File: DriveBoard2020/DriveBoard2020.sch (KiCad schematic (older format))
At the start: 3 parts

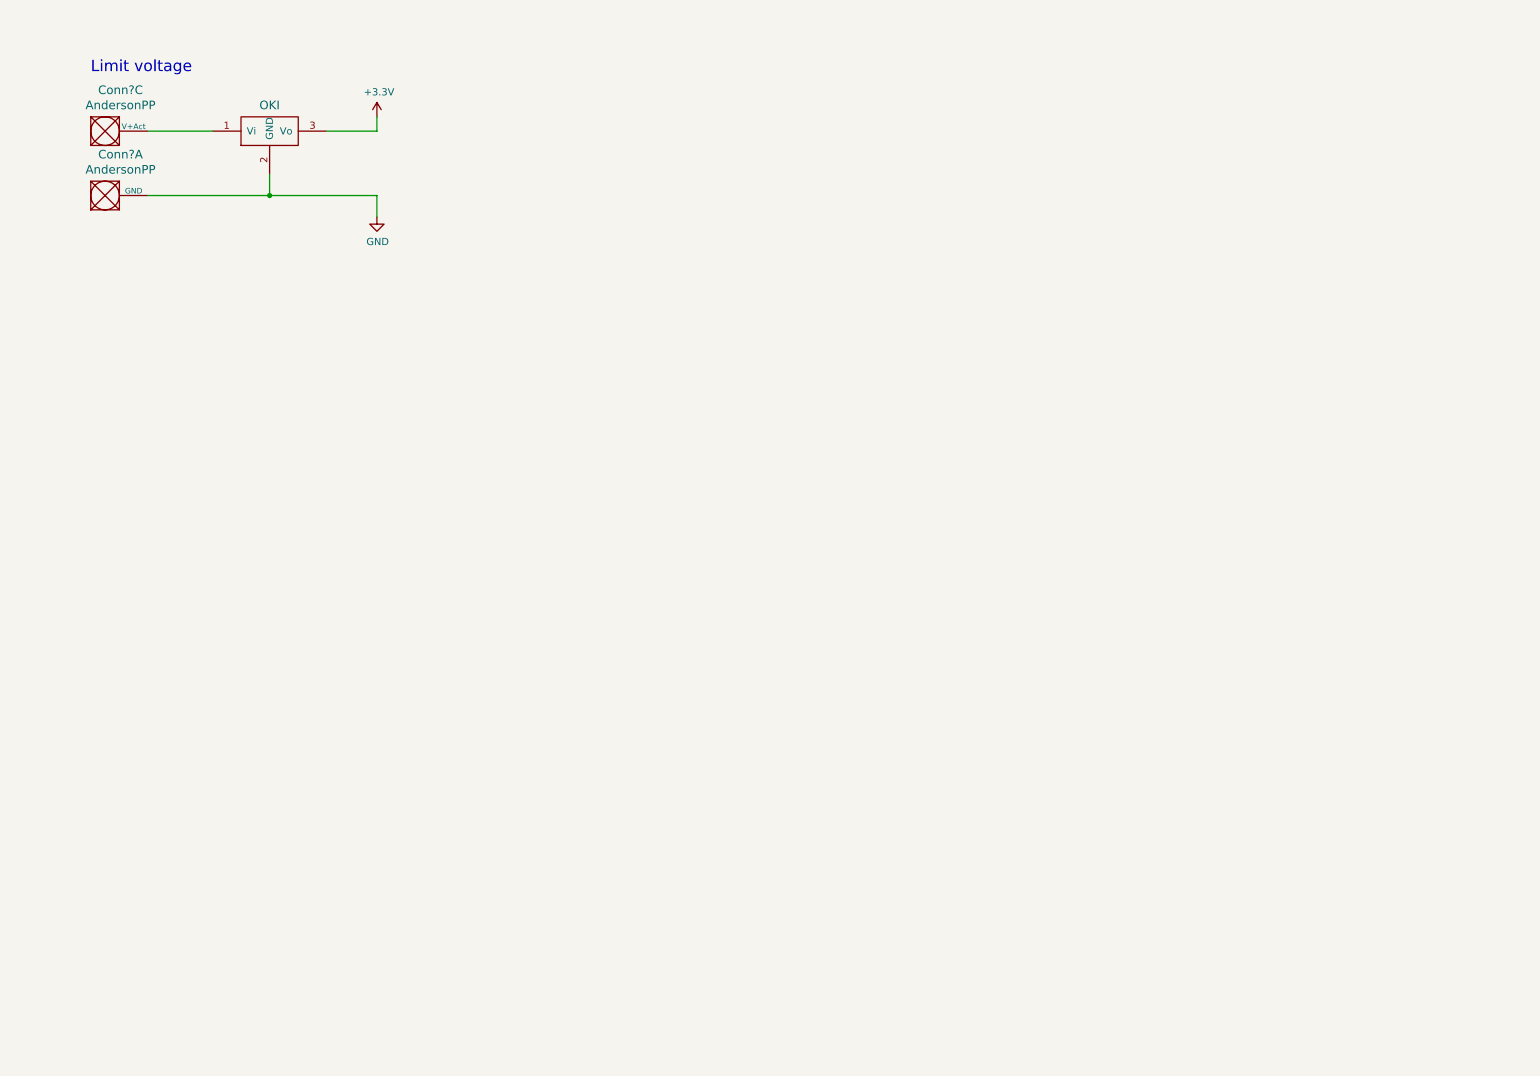
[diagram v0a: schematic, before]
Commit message: Fixed level shifters using 323s, connected molex
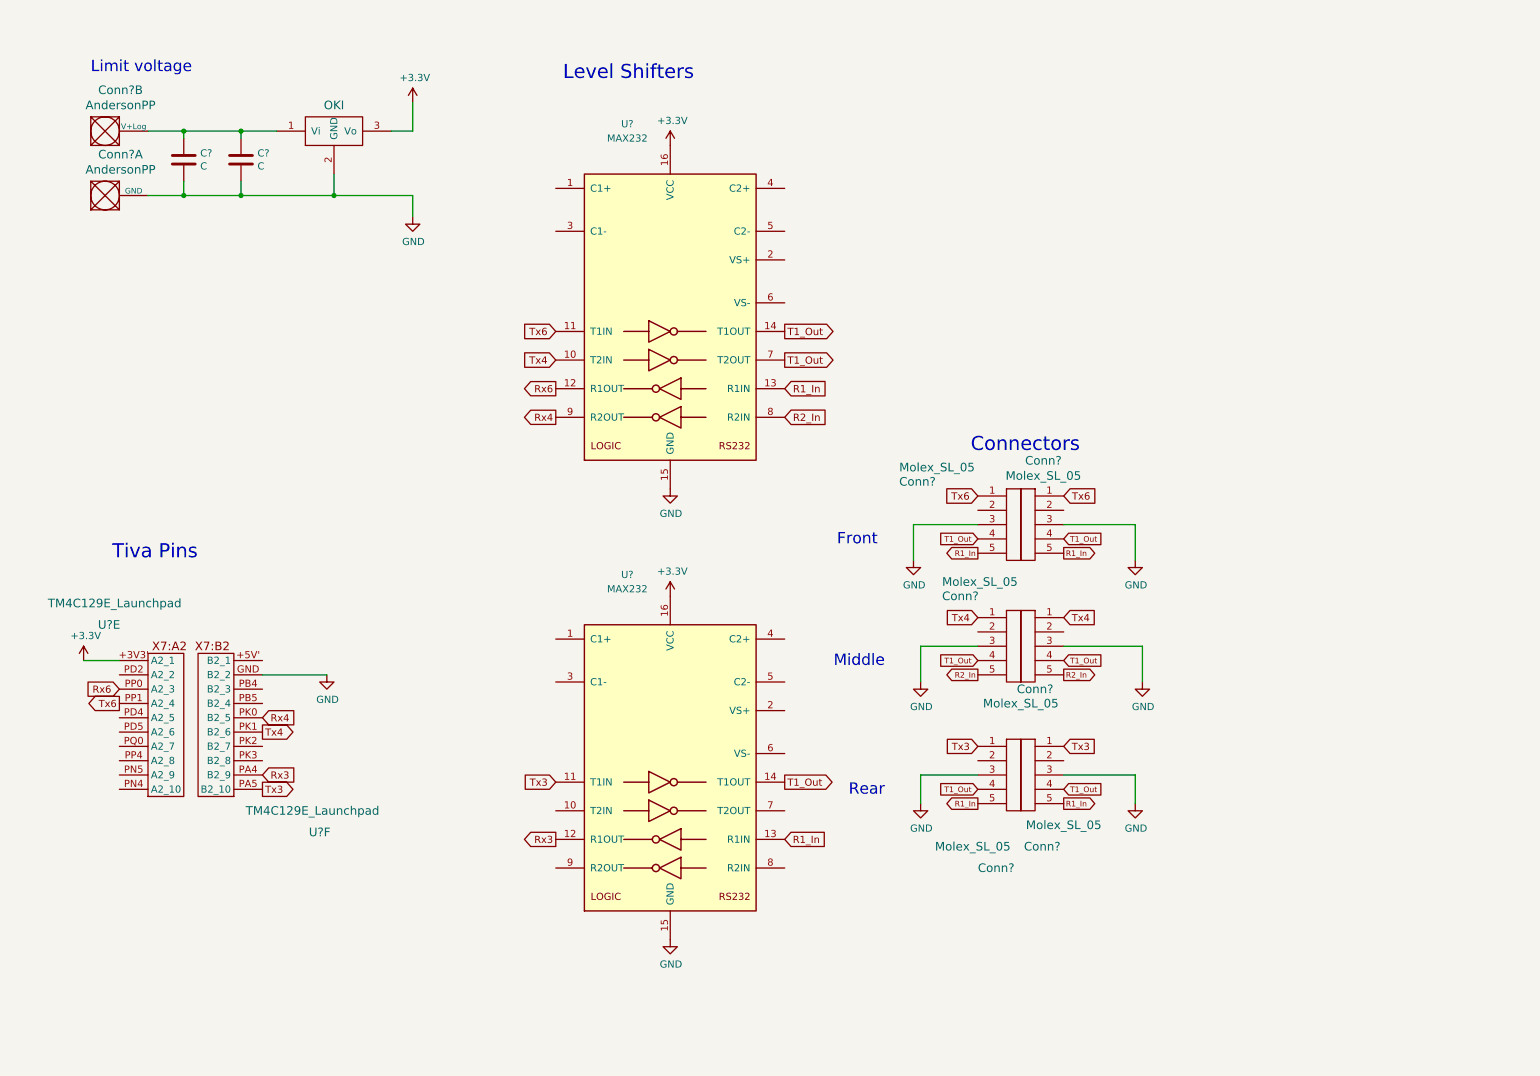
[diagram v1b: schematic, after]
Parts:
- removed Conn?: AndersonPP, symbol MRDT_Connectors:AndersonPP
- added C? (x2): C, symbol Device:C
- added Conn? (x6): Molex_SL_05, symbol MRDT_Connectors:Molex_SL_05
- added Conn?: AndersonPP, symbol MRDT_Connectors:AndersonPP
- added U? (x2): TM4C129E_Launchpad, symbol MRDT_Shields:TM4C129E_Launchpad
- added U? (x2): MAX232, symbol Interface_UART:MAX232
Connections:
- net +3V3: now also U?.+3V3' (A2_1), U?.16 (VCC), U?.16 (VCC)
- net GND: now also C?.2, C?.2, Conn?.3, Conn?.3, Conn?.3, Conn?.3, Conn?.3, Conn?.3, U?.15 (GND), U?.15 (GND), U?.GND (B2_2)
- net at U?.1 (Vi): now also C?.1, C?.1, Conn?.2 (V+Log)
- new net R1_In: Conn?.5, Conn?.5, Conn?.5, Conn?.5, U?.13 (R1IN), U?.13 (R1IN)
- new net R2_In: Conn?.5, Conn?.5, U?.8 (R2IN)
- new net Rx3: U?.12 (R1OUT), U?.PA4 (B2_9)
- new net Rx4: U?.9 (R2OUT), U?.PK0 (B2_5)
- new net Rx6: U?.12 (R1OUT), U?.PP0 (A2_3)
- new net T1_Out: Conn?.4, Conn?.4, Conn?.4, Conn?.4, Conn?.4, Conn?.4, U?.14 (T1OUT), U?.14 (T1OUT), U?.7 (T2OUT)
- new net Tx3: Conn?.1, Conn?.1, U?.11 (T1IN), U?.PA5 (B2_10)
- new net Tx4: Conn?.1, Conn?.1, U?.10 (T2IN), U?.PK1 (B2_6)
- new net Tx6: Conn?.1, Conn?.1, U?.11 (T1IN), U?.PP1 (A2_4)
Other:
- note added: "Connectors"
- note added: "Front"
- note added: "Level Shifters"
- note added: "Middle"
- note added: "Rear"
- note added: "Tiva Pins"

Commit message: organized schematic
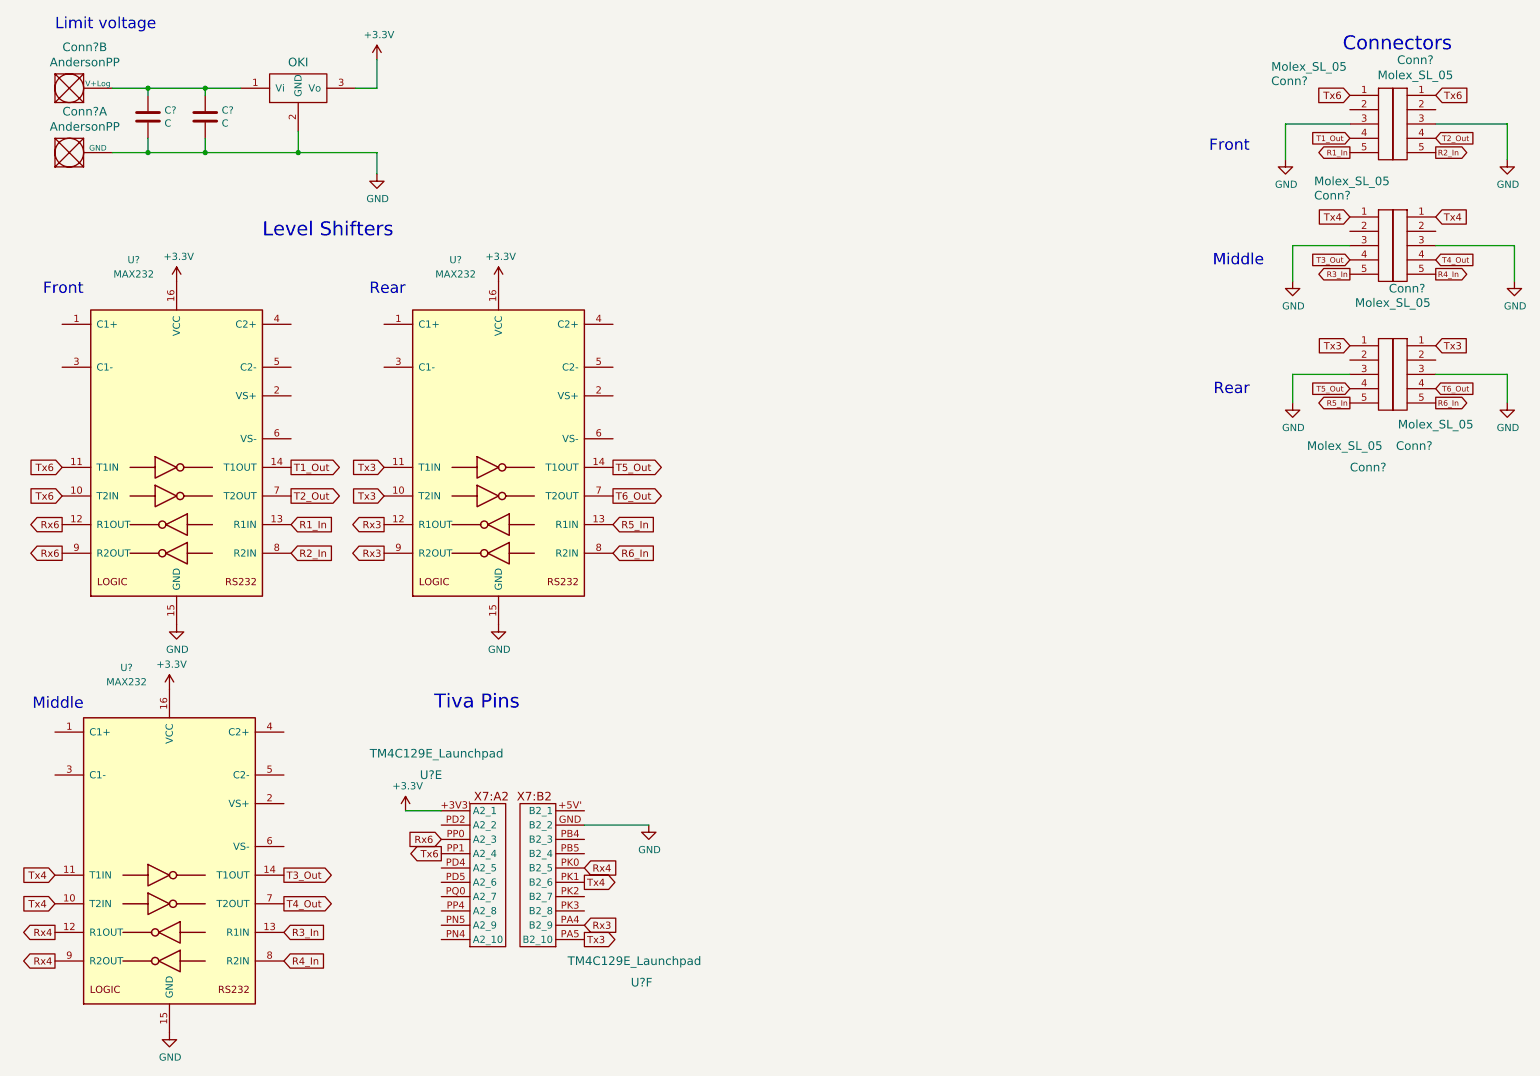
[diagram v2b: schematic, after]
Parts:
- added U?: MAX232, symbol Interface_UART:MAX232
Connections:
- net +3V3: now also U?.16 (VCC)
- net GND: now also U?.15 (GND)
- net R1_In: no longer Conn?.5, Conn?.5, Conn?.5, U?.13 (R1IN)
- net R2_In: now also Conn?.5; no longer Conn?.5, Conn?.5
- net Rx3: now also U?.12 (R1OUT), U?.9 (R2OUT); no longer U?.12 (R1OUT)
- net Rx4: now also U?.12 (R1OUT), U?.9 (R2OUT); no longer U?.9 (R2OUT)
- net Rx6: now also U?.9 (R2OUT)
- net T1_Out: no longer Conn?.4, Conn?.4, Conn?.4, Conn?.4, Conn?.4, U?.14 (T1OUT), U?.7 (T2OUT)
- net Tx3: now also U?.10 (T2IN), U?.11 (T1IN); no longer U?.11 (T1IN)
- net Tx4: now also U?.10 (T2IN), U?.11 (T1IN); no longer U?.10 (T2IN)
- net Tx6: now also U?.10 (T2IN)
- net T4_Out: now reaches U?.7 (T2OUT)
- net T4_Out: now also Conn?.4
- net R4_In: now reaches U?.8 (R2IN)
- net R4_In: now also Conn?.5
- new net R3_In: Conn?.5, U?.13 (R1IN)
- new net R5_In: Conn?.5, U?.13 (R1IN)
- new net R6_In: Conn?.5, U?.8 (R2IN)
- new net T2_Out: Conn?.4, U?.7 (T2OUT)
- new net T3_Out: Conn?.4, U?.14 (T1OUT)
- new net T5_Out: Conn?.4, U?.14 (T1OUT)
- new net T6_Out: Conn?.4, U?.7 (T2OUT)
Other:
- moved on the sheet: C?, Conn?, Conn?A, Conn?B, U?, U?E, U?F

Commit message: added LED's
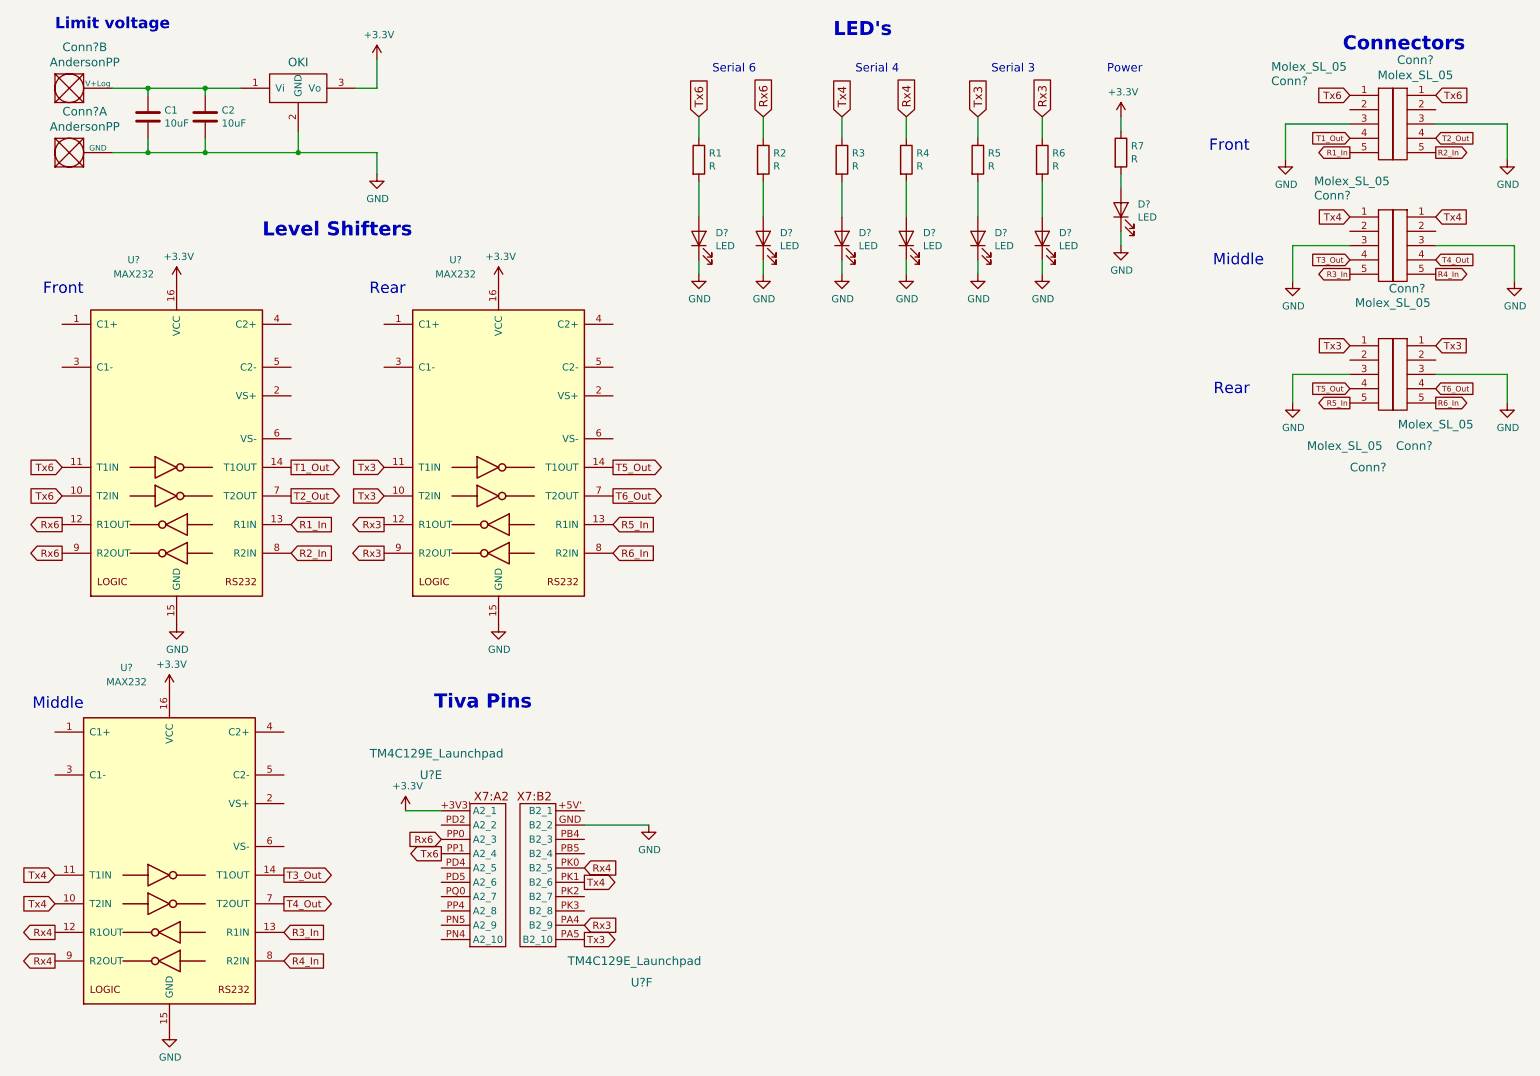
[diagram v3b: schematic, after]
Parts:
- added D? (x7): LED, symbol Device:LED
- added R1, R2, R3, R4, R5, R6, R7: R, symbol Device:R
- C1, C2: renamed from C?; value C -> 10uF
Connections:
- net +3V3: now also R7.1
- net GND: now also D?.1 (K), D?.1 (K), D?.1 (K), D?.1 (K), D?.1 (K), D?.1 (K), D?.1 (K)
- net Rx3: now also R6.1
- net Rx4: now also R4.1
- net Rx6: now also R2.1
- net Tx3: now also R5.1
- net Tx4: now also R3.1
- net Tx6: now also R1.1
- new net: D?.2 (A), R1.2
- new net: D?.2 (A), R2.2
- new net: D?.2 (A), R3.2
- new net: D?.2 (A), R4.2
- new net: D?.2 (A), R5.2
- new net: D?.2 (A), R6.2
- new net: D?.2 (A), R7.2
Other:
- note added: "LED's"
- note added: "Power"
- note added: "Serial 3"
- note added: "Serial 4"
- note added: "Serial 6"
